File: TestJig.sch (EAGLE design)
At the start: 18 parts

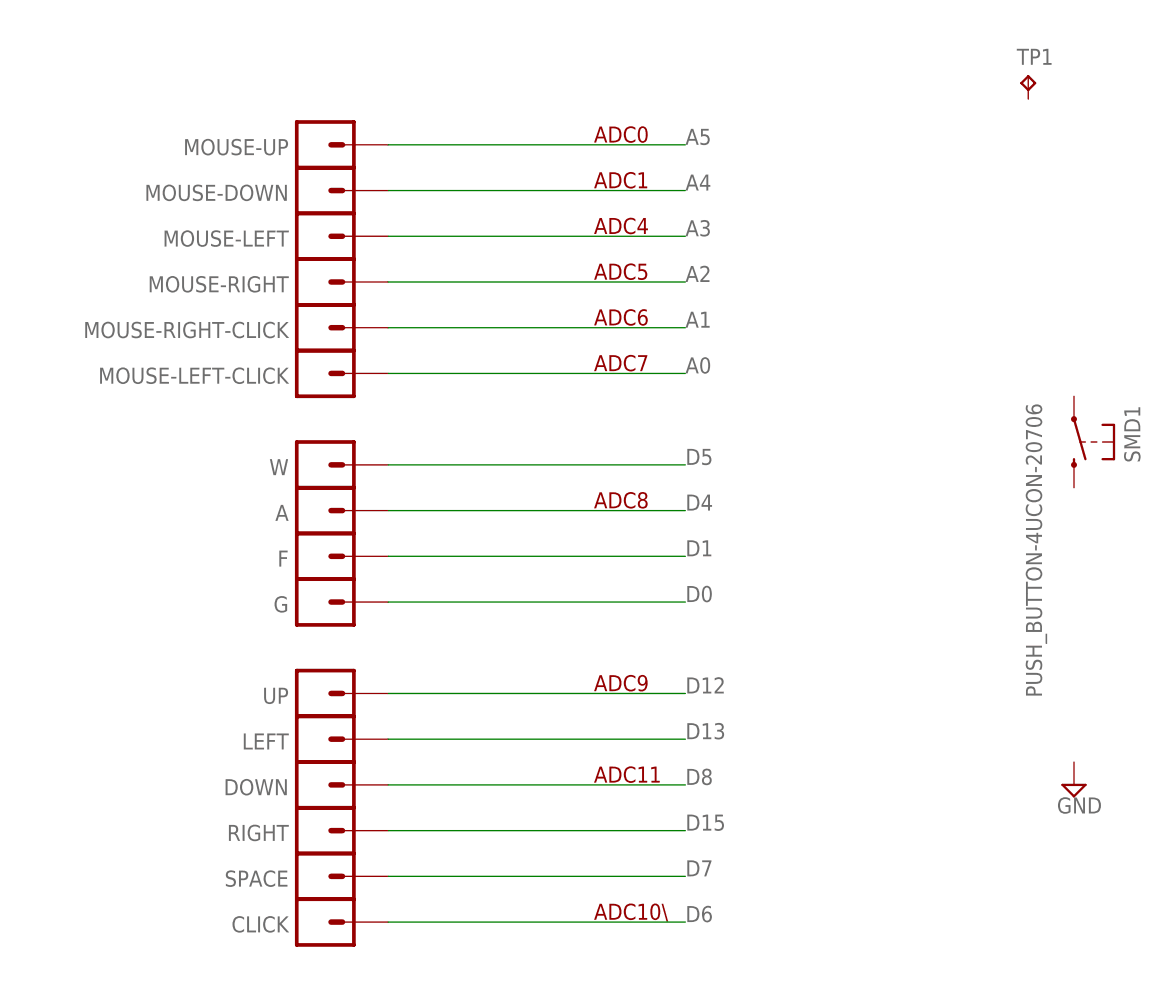
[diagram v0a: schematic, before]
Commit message: added Production test folder
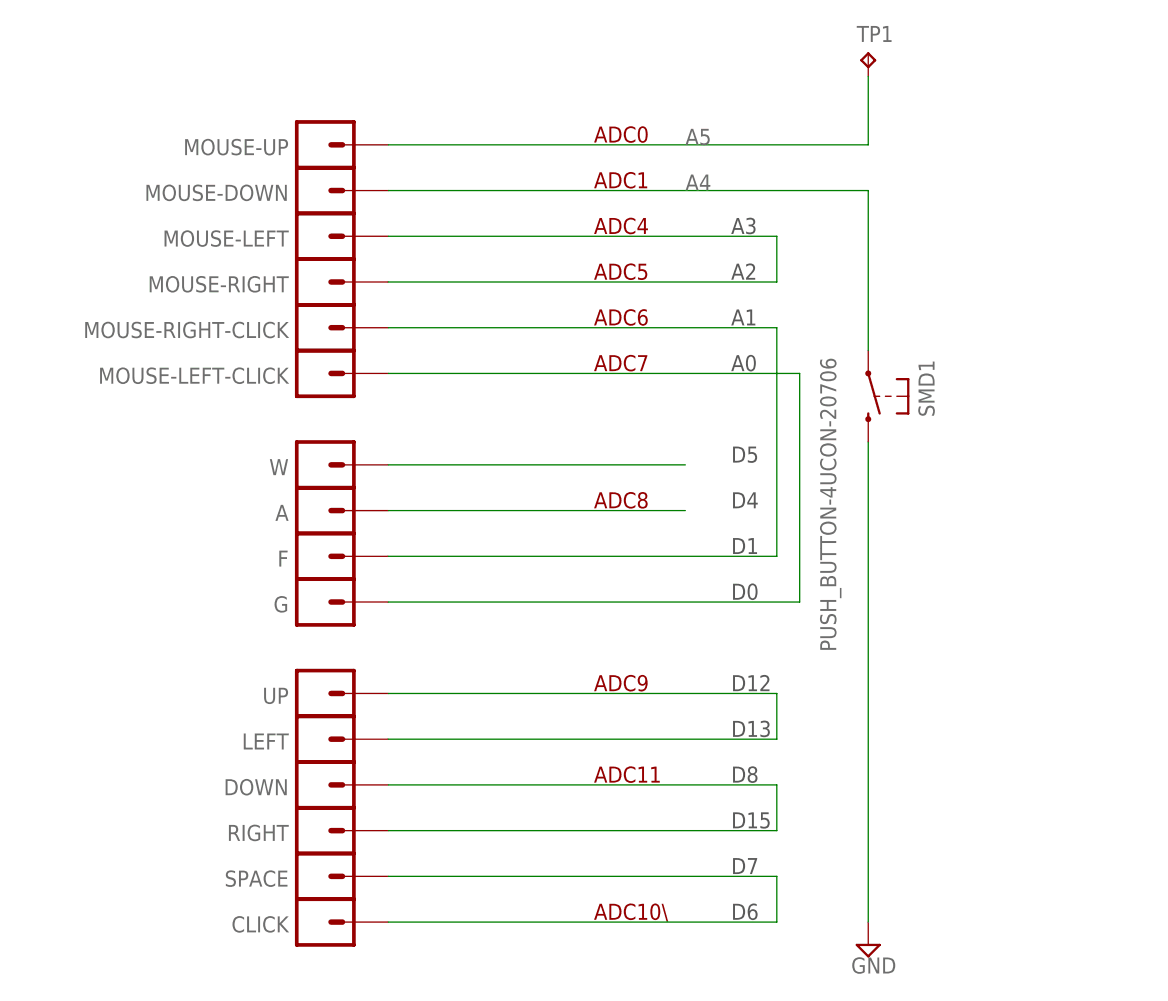
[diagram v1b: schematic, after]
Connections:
- removed net A2: MOUSE-RIGHT.1
- removed net D0: G.1
- removed net D1: F.1
- removed net D13: LEFT.1
- removed net D15: RIGHT.1
- removed net D6: CLICK.1
- new net GND: SMD1.2
- net A0: now also G.1
- net A1: now also F.1
- net A3: now also MOUSE-RIGHT.1
- net A4: now also SMD1.1
- net A5: now also TP1.TP
- net D12: now also LEFT.1
- net D7: now also CLICK.1
- net D8: now also RIGHT.1
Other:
- note added: "A0"
- note added: "A1"
- note added: "A2"
- note added: "A3"
- note added: "D0"
- note added: "D1"
- note added: "D12"
- note added: "D13"
- note added: "D15"
- note added: "D4"
- note added: "D5"
- note added: "D6"
- note added: "D7"
- note added: "D8"
- moved on the sheet: SMD1, TP1
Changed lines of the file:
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@@
 <setting verticaltext="up"/>
 </settings>
-<grid distance="0.1" unitdist="inch" unit="inch" style="lines" multiple="1" display="yes" altdistance="0.01" altunitdist="inch" altunit="inch"/>
+<grid distance="0.1" unitdist="inch" unit="inch" style="lines" multiple="1" display="no" altdistance="0.01" altunitdist="inch" altunit="inch"/>
 <layers>
 <layer number="1" name="Top" color="4" fill="1" visible="no" active="no"/>
@@
 <text x="40.64" y="99.314" size="1.778" layer="94">ADC1</text>
 <text x="40.64" y="104.394" size="1.778" layer="94">ADC0</text>
+<text x="55.88" y="94.234" size="1.778" layer="97">A3</text>
+<text x="55.88" y="89.154" size="1.778" layer="97">A2</text>
+<text x="55.88" y="84.074" size="1.778" layer="97">A1</text>
+<text x="55.88" y="78.994" size="1.778" layer="97">A0</text>
+<text x="55.88" y="68.834" size="1.778" layer="97">D5</text>
+<text x="55.88" y="63.754" size="1.778" layer="97">D4</text>
+<text x="55.88" y="58.674" size="1.778" layer="97">D1</text>
+<text x="55.88" y="53.594" size="1.778" layer="97">D0</text>
+<text x="55.88" y="43.434" size="1.778" layer="97">D12</text>
+<text x="55.88" y="38.354" size="1.778" layer="97">D13</text>
+<text x="55.88" y="33.274" size="1.778" layer="97">D8</text>
+<text x="55.88" y="28.194" size="1.778" layer="97">D15</text>
+<text x="55.88" y="23.114" size="1.778" layer="97">D7</text>
+<text x="55.88" y="18.034" size="1.778" layer="97">D6</text>
 </plain>
 <instances>
@@
 <attribute name="NAME" x="6.731" y="104.775" size="1.778" layer="95" rot="R180"/>
 </instance>
-<instance part="TP1" gate="G$1" x="88.9" y="111.76"/>
-<instance part="SMD1" gate="G$1" x="96.52" y="71.12" rot="R270"/>
-<instance part="SUPPLY1" gate="GND" x="93.98" y="33.02"/>
+<instance part="TP1" gate="G$1" x="71.12" y="114.3"/>
+<instance part="SMD1" gate="G$1" x="73.66" y="76.2" rot="R270"/>
+<instance part="SUPPLY1" gate="GND" x="71.12" y="15.24"/>
 </instances>
 <busses>
@@
 <segment>
 <pinref part="UP" gate="G$1" pin="1"/>
-<wire x1="17.78" y1="43.18" x2="50.8" y2="43.18" width="0.1524" layer="91"/>
-<label x="50.8" y="43.18" size="1.778" layer="95"/>
-</segment>
-</net>
-<net name="D13" class="0">
-<segment>
+<wire x1="17.78" y1="43.18" x2="60.96" y2="43.18" width="0.1524" layer="91"/>
+<wire x1="60.96" y1="43.18" x2="60.96" y2="38.1" width="0.1524" layer="91"/>
 <pinref part="LEFT" gate="G$1" pin="1"/>
-<wire x1="17.78" y1="38.1" x2="50.8" y2="38.1" width="0.1524" layer="91"/>
-<label x="50.8" y="38.1" size="1.778" layer="95"/>
+<wire x1="17.78" y1="38.1" x2="60.96" y2="38.1" width="0.1524" layer="91"/>
 </segment>
 </net>
@@
 <segment>
 <pinref part="DOWN" gate="G$1" pin="1"/>
-<wire x1="17.78" y1="33.02" x2="50.8" y2="33.02" width="0.1524" layer="91"/>
-<label x="50.8" y="33.02" size="1.778" layer="95"/>
-</segment>
-</net>
-<net name="D15" class="0">
-<segment>
+<wire x1="17.78" y1="33.02" x2="60.96" y2="33.02" width="0.1524" layer="91"/>
+<wire x1="60.96" y1="33.02" x2="60.96" y2="27.94" width="0.1524" layer="91"/>
 <pinref part="RIGHT" gate="G$1" pin="1"/>
-<wire x1="17.78" y1="27.94" x2="50.8" y2="27.94" width="0.1524" layer="91"/>
-<label x="50.8" y="27.94" size="1.778" layer="95"/>
+<wire x1="17.78" y1="27.94" x2="60.96" y2="27.94" width="0.1524" layer="91"/>
 </segment>
 </net>
@@
 <segment>
 <pinref part="SPACE" gate="G$1" pin="1"/>
-<wire x1="17.78" y1="22.86" x2="50.8" y2="22.86" width="0.1524" layer="91"/>
-<label x="50.8" y="22.86" size="1.778" layer="95"/>
-</segment>
-</net>
-<net name="D6" class="0">
-<segment>
+<wire x1="17.78" y1="22.86" x2="60.96" y2="22.86" width="0.1524" layer="91"/>
+<wire x1="60.96" y1="22.86" x2="60.96" y2="17.78" width="0.1524" layer="91"/>
 <pinref part="CLICK" gate="G$1" pin="1"/>
-<wire x1="17.78" y1="17.78" x2="50.8" y2="17.78" width="0.1524" layer="91"/>
-<label x="50.8" y="17.78" size="1.778" layer="95"/>
+<wire x1="17.78" y1="17.78" x2="60.96" y2="17.78" width="0.1524" layer="91"/>
 </segment>
 </net>
@@
 <segment>
 <pinref part="W" gate="G$1" pin="1"/>
-<label x="50.8" y="68.58" size="1.778" layer="95"/>
 <wire x1="17.78" y1="68.58" x2="50.8" y2="68.58" width="0.1524" layer="91"/>
 </segment>
@@
 <segment>
 <pinref part="A" gate="G$1" pin="1"/>
-<label x="50.8" y="63.5" size="1.778" layer="95"/>
 <wire x1="17.78" y1="63.5" x2="50.8" y2="63.5" width="0.1524" layer="91"/>
-</segment>
-</net>
-<net name="D1" class="0">
-<segment>
-<pinref part="F" gate="G$1" pin="1"/>
-<wire x1="17.78" y1="58.42" x2="50.8" y2="58.42" width="0.1524" layer="91"/>
-<label x="50.8" y="58.42" size="1.778" layer="95"/>
-</segment>
-</net>
-<net name="D0" class="0">
-<segment>
-<pinref part="G" gate="G$1" pin="1"/>
-<wire x1="17.78" y1="53.34" x2="50.8" y2="53.34" width="0.1524" layer="91"/>
-<label x="50.8" y="53.34" size="1.778" layer="95"/>
 </segment>
 </net>
@@
 <pinref part="MOUSE-UP" gate="G$1" pin="1"/>
 <label x="50.8" y="104.14" size="1.778" layer="95"/>
-<wire x1="17.78" y1="104.14" x2="50.8" y2="104.14" width="0.1524" layer="91"/>
+<pinref part="TP1" gate="G$1" pin="TP"/>
+<wire x1="17.78" y1="104.14" x2="71.12" y2="104.14" width="0.1524" layer="91"/>
+<wire x1="71.12" y1="104.14" x2="71.12" y2="111.76" width="0.1524" layer="91"/>
 </segment>
 </net>
@@
 <pinref part="MOUSE-DOWN" gate="G$1" pin="1"/>
 <label x="50.8" y="99.06" size="1.778" layer="95"/>
-<wire x1="17.78" y1="99.06" x2="50.8" y2="99.06" width="0.1524" layer="91"/>
+<pinref part="SMD1" gate="G$1" pin="1"/>
+<wire x1="17.78" y1="99.06" x2="71.12" y2="99.06" width="0.1524" layer="91"/>
+<wire x1="71.12" y1="99.06" x2="71.12" y2="81.28" width="0.1524" layer="91"/>
 </segment>
 </net>
@@
 <segment>
 <pinref part="MOUSE-LEFT" gate="G$1" pin="1"/>
-<label x="50.8" y="93.98" size="1.778" layer="95"/>
-<wire x1="17.78" y1="93.98" x2="50.8" y2="93.98" width="0.1524" layer="91"/>
-</segment>
-</net>
-<net name="A2" class="0">
-<segment>
+<wire x1="17.78" y1="93.98" x2="60.96" y2="93.98" width="0.1524" layer="91"/>
+<wire x1="60.96" y1="93.98" x2="60.96" y2="88.9" width="0.1524" layer="91"/>
 <pinref part="MOUSE-RIGHT" gate="G$1" pin="1"/>
-<wire x1="17.78" y1="88.9" x2="50.8" y2="88.9" width="0.1524" layer="91"/>
-<label x="50.8" y="88.9" size="1.778" layer="95"/>
+<wire x1="17.78" y1="88.9" x2="60.96" y2="88.9" width="0.1524" layer="91"/>
 </segment>
 </net>
@@
 <segment>
 <pinref part="MOUSE-RIGHT-CLICK" gate="G$1" pin="1"/>
-<wire x1="17.78" y1="83.82" x2="50.8" y2="83.82" width="0.1524" layer="91"/>
-<label x="50.8" y="83.82" size="1.778" layer="95"/>
+<wire x1="17.78" y1="83.82" x2="60.96" y2="83.82" width="0.1524" layer="91"/>
+<wire x1="60.96" y1="83.82" x2="60.96" y2="58.42" width="0.1524" layer="91"/>
+<pinref part="F" gate="G$1" pin="1"/>
+<wire x1="17.78" y1="58.42" x2="60.96" y2="58.42" width="0.1524" layer="91"/>
 </segment>
 </net>
@@
 <segment>
 <pinref part="MOUSE-LEFT-CLICK" gate="G$1" pin="1"/>
-<wire x1="17.78" y1="78.74" x2="50.8" y2="78.74" width="0.1524" layer="91"/>
-<label x="50.8" y="78.74" size="1.778" layer="95"/>
-</segment>
-</net>
+<wire x1="17.78" y1="78.74" x2="63.5" y2="78.74" width="0.1524" layer="91"/>
+<wire x1="63.5" y1="78.74" x2="63.5" y2="53.34" width="0.1524" layer="91"/>
+<pinref part="G" gate="G$1" pin="1"/>
+<wire x1="17.78" y1="53.34" x2="63.5" y2="53.34" width="0.1524" layer="91"/>
+</segment>
+</net>
+<net name="GND" class="0">
+<segment>
+<pinref part="SMD1" gate="G$1" pin="2"/>
+<pinref part="SUPPLY1" gate="GND" pin="GND"/>
+<wire x1="71.12" y1="71.12" x2="71.12" y2="17.78" width="0.1524" layer="91"/>
+</segment>
+</net>

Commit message: changed name to ShakeUp
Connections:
- removed net D4: A.1
- net D5: now also A.1
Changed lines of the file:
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@@
 <setting verticaltext="up"/>
 </settings>
-<grid distance="0.1" unitdist="inch" unit="inch" style="lines" multiple="1" display="no" altdistance="0.01" altunitdist="inch" altunit="inch"/>
+<grid distance="0.1" unitdist="inch" unit="inch" style="lines" multiple="1" display="yes" altdistance="0.01" altunitdist="inch" altunit="inch"/>
 <layers>
 <layer number="1" name="Top" color="4" fill="1" visible="no" active="no"/>
@@
 <segment>
 <pinref part="W" gate="G$1" pin="1"/>
-<wire x1="17.78" y1="68.58" x2="50.8" y2="68.58" width="0.1524" layer="91"/>
+<wire x1="17.78" y1="68.58" x2="53.34" y2="68.58" width="0.1524" layer="91"/>
+<wire x1="53.34" y1="68.58" x2="53.34" y2="63.5" width="0.1524" layer="91"/>
+<pinref part="A" gate="G$1" pin="1"/>
+<wire x1="17.78" y1="63.5" x2="53.34" y2="63.5" width="0.1524" layer="91"/>
 </segment>
 </net>
-<net name="D4" class="0">
-<segment>
-<pinref part="A" gate="G$1" pin="1"/>
-<wire x1="17.78" y1="63.5" x2="50.8" y2="63.5" width="0.1524" layer="91"/>
-</segment>
-</net>
